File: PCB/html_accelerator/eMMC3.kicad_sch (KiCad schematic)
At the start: 15 parts, among them U6 EMMC_4G, U7 EMMC_4G, U9 AU6438BS, Y4 12MHz

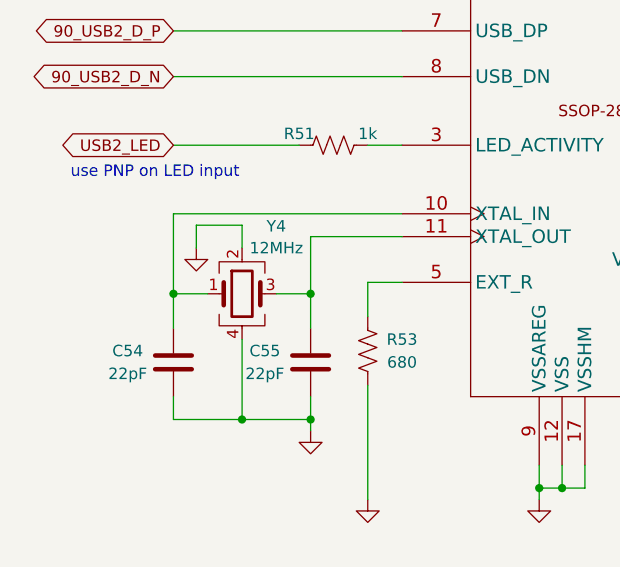
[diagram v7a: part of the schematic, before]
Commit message: Additional routing greebles, cleanup and gerber export with BOM
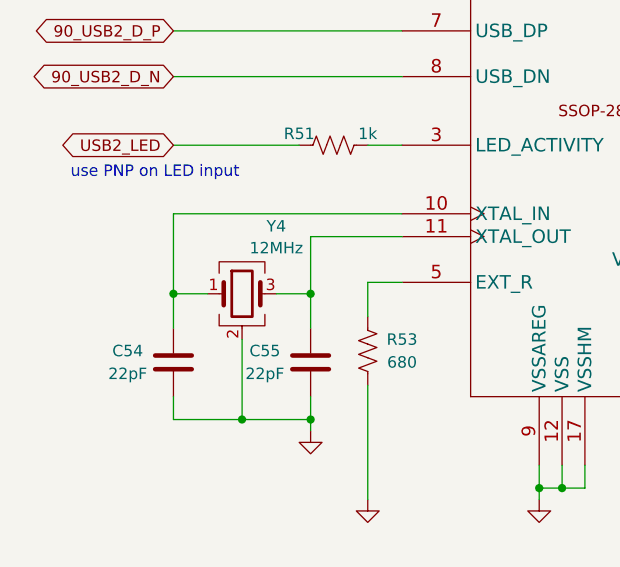
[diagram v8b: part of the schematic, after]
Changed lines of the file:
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@@
-	(wire
-		(pts
-			(xy 41.91 87.63) (xy 36.83 87.63)
-		)
-		(stroke
-			(width 0)
-			(type default)
-		)
-	)
 	(wire
 		(pts
@@
 	(wire
 		(pts
-			(xy 41.91 90.17) (xy 41.91 87.63)
-		)
-		(stroke
-			(width 0)
-			(type default)
-		)
-	)
-	(wire
-		(pts
 			(xy 140.97 81.28) (xy 148.59 81.28)
 		)
@@
 		(pts
 			(xy 118.11 91.44) (xy 118.11 88.9)
-		)
-		(stroke
-			(width 0)
-			(type default)
-		)
-	)
-	(wire
-		(pts
-			(xy 36.83 87.63) (xy 36.83 90.17)
 		)
 		(stroke
@@
 			)
 		)
-		(property "Description" ""
+		(property "Description" "Four pin crystal, GND on pins 2 and 4"
 			(at 41.91 95.25 0)
+			(hide yes)
 			(show_name no)
 			(do_not_autoplace no)
@@
 				)
 			)
-		)
-	)
-	(symbol
-		(lib_id "power:GND")
-		(at 36.83 90.17 0)
-		(unit 1)
-		(body_style 1)
-		(exclude_from_sim no)
-		(in_bom yes)
-		(on_board yes)
-		(in_pos_files yes)
-		(dnp no)
-		(fields_autoplaced yes)
-		(property "Reference" "#PWR058"
-			(at 36.83 96.52 0)
-			(hide yes)
-			(show_name no)
-			(do_not_autoplace no)
-			(effects
-				(font
-					(size 1.27 1.27)
-				)
-			)
-		)
-		(property "Value" "GND"
-			(at 36.83 94.3055 0)
-			(hide yes)
-			(show_name no)
-			(do_not_autoplace no)
-			(effects
-				(font
-					(size 1.27 1.27)
-				)
-			)
-		)
-		(property "Footprint" ""
-			(at 36.83 90.17 0)
-			(hide yes)
-			(show_name no)
-			(do_not_autoplace no)
-			(effects
-				(font
-					(size 1.27 1.27)
-				)
-			)
-		)
-		(property "Datasheet" ""
-			(at 36.83 90.17 0)
-			(hide yes)
-			(show_name no)
-			(do_not_autoplace no)
-			(effects
-				(font
-					(size 1.27 1.27)
-				)
-			)
-		)
-		(property "Description" ""
-			(at 36.83 90.17 0)
-			(show_name no)
-			(do_not_autoplace no)
-			(effects
-				(font
-					(size 1.27 1.27)
-				)
-			)
-		)
-		(pin "1"
-		)
-		(instances
-			(project "html_accelerator"
-				(path "/12b3a7c9-141f-40ba-9ebb-094b58bfa6c7/e4cf78dc-8e0c-4eaf-ac6f-547ec39b6f59"
-					(reference "#PWR058")
-					(unit 1)
-				)
-			)
